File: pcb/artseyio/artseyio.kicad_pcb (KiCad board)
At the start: 2 copper layers, 95.2 x 69.9 mm, 14 parts, among them SW1 SW_MEC_5G, SW2 SW_MEC_5G, SW3 SW_MEC_5G, SW4 SW_MEC_5G, SW5 SW_MEC_5G, SW6 SW_MEC_5G, SW7 SW_MEC_5G, SW8 SW_MEC_5G, U1 RP2040-Zero, U2 mini_esp32

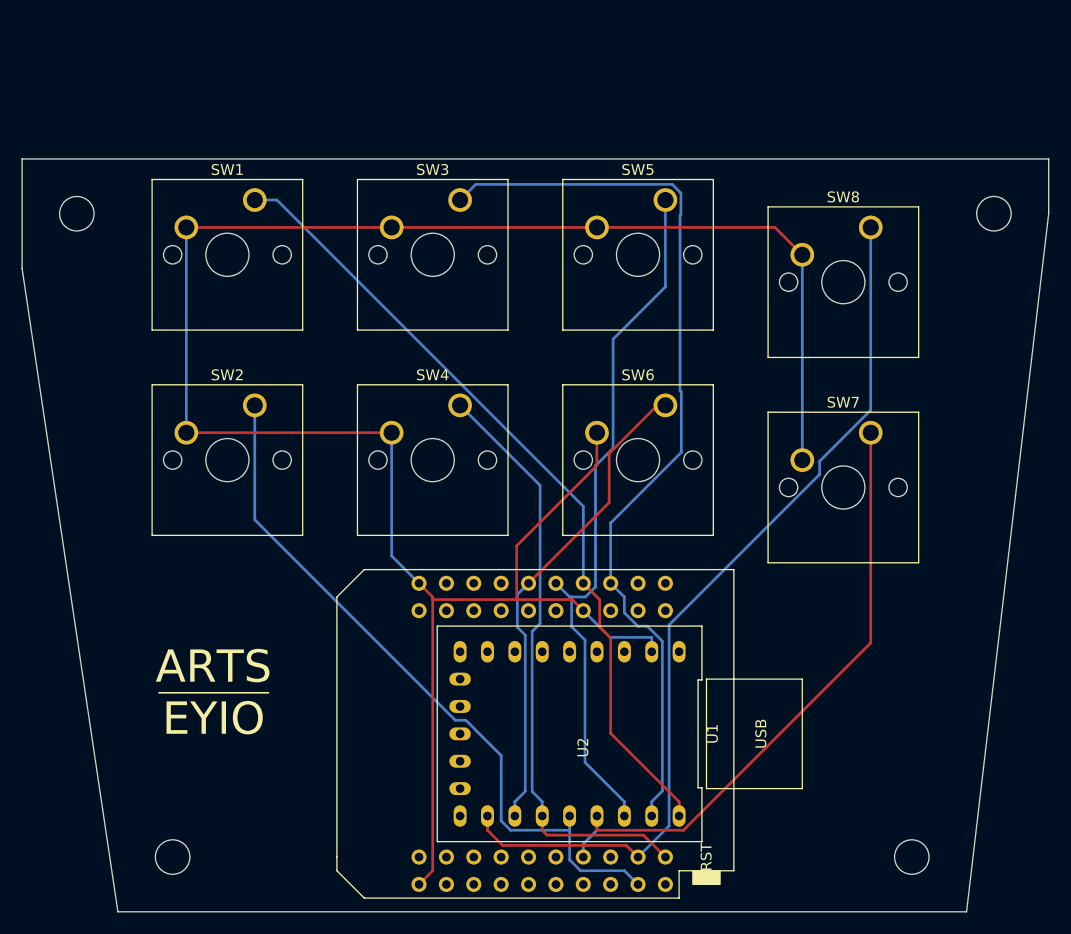
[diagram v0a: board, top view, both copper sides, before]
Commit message: Updated schematic to include  a CH552 with builtin USB-C port.
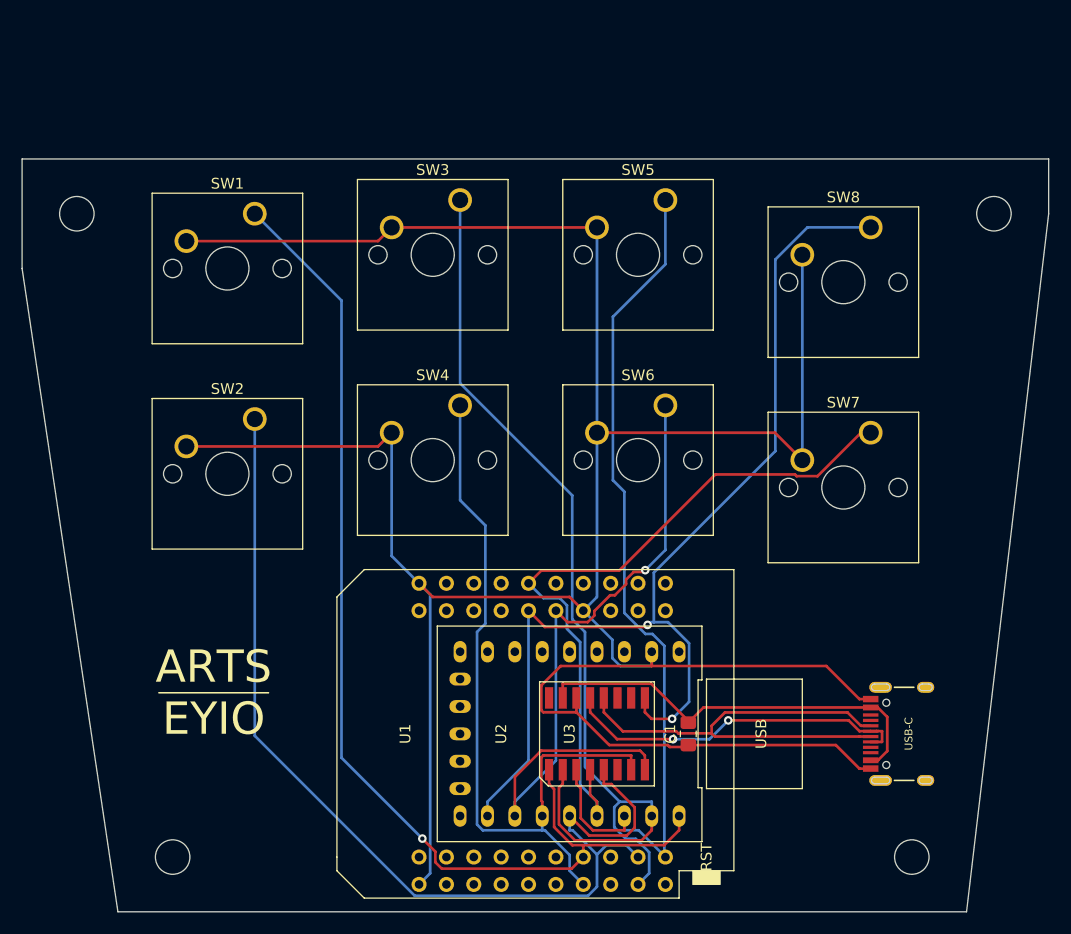
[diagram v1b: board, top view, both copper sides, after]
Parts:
- added C1: C, Capacitor_SMD:C_0805_2012Metric_Pad1.18x1.45mm_HandSolder, F.Cu at (168.5, 118.1)
- added J1: USB_C16PIN, USB-C:USB-C-COM-15111, F.Cu at (185.4, 118.1)
- added U3: CH552G, CH552G:CH552G, F.Cu at (160.0, 118.1)
- moved SW2 1.27 mm to (128.3, 88.9)
- moved SW1 1.27 mm to (128.3, 69.8)
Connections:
- U2 pad 13: unconnected-(U2-Pad13) -> /Y
- U2 pad 14: /S -> /A
- U2 pad 17: /E -> /R
- U2 pad 18: /O -> /E
- U2 pad 20: /Y -> /T
- U2 pad 29: unconnected-(U2-Pad29) -> /O
- U2 pad 30: /I -> /S
- U2 pad 31: unconnected-(U2-Pad31) -> /I
- U2 pad 32: /T -> unconnected-(U2-Pad32)
- U2 pad 34: /A -> unconnected-(U2-Pad34)
- U2 pad 36: /R -> unconnected-(U2-Pad36)
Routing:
- net Earth: track 201.0 -> 274.8 mm
- net Net-(J1-PadA6): track 0.00 -> 43.5 mm
- net Net-(C1-Pad2): track 0.00 -> 39.0 mm
- net Net-(J1-PadA7): track 0.00 -> 32.6 mm, vias 0 -> 2
- net /A: track 74.7 -> 102.3 mm, vias 0 -> 1
- net /E: track 66.7 -> 94.1 mm
- net /I: track 44.9 -> 66.1 mm, vias 0 -> 1
- net /T: track 65.5 -> 82.0 mm
- net /Y: track 55.7 -> 69.7 mm
- net /O: track 83.7 -> 97.3 mm, vias 0 -> 2
- net /S: track 57.8 -> 67.3 mm
- net /R: track 84.9 -> 92.6 mm

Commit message: Updated the footprint shape and updated the ESP32 pinout.
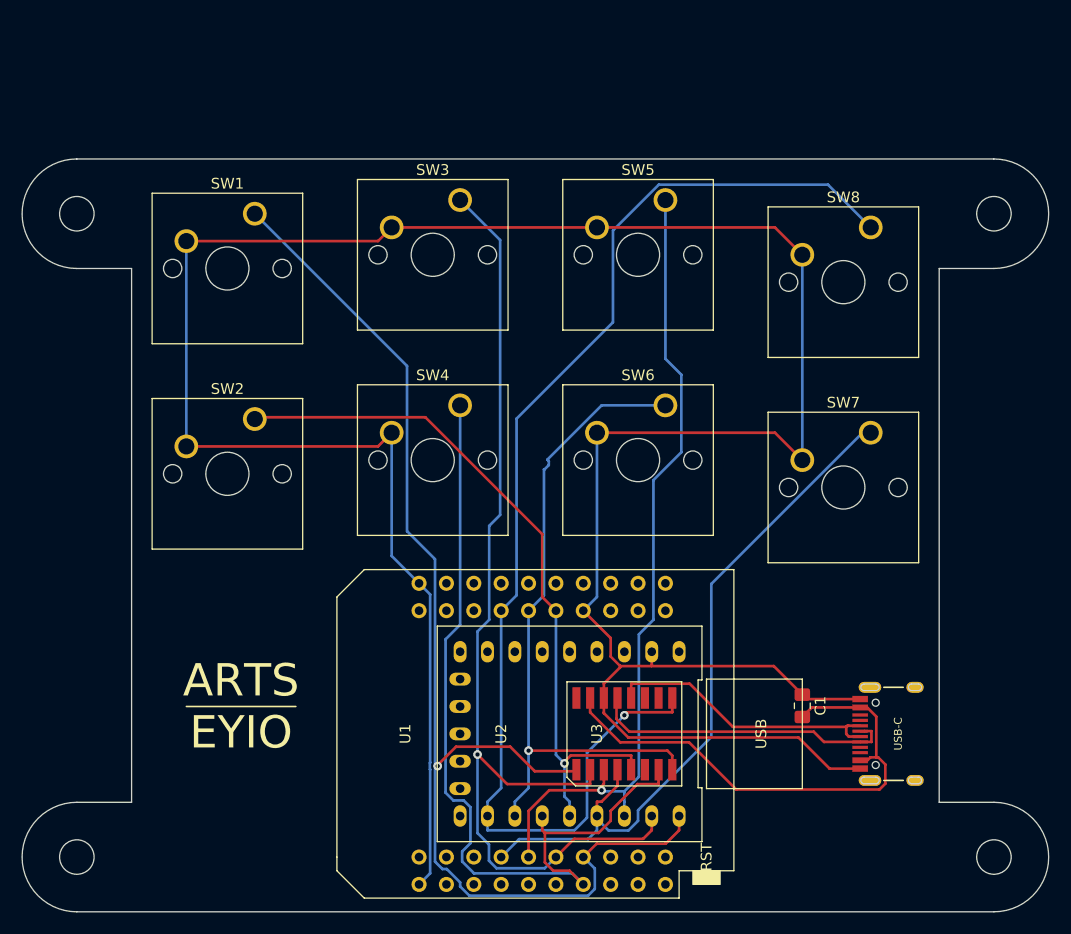
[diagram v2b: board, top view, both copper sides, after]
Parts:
- C1: value C -> 0.1uF
- moved C1 10.9 mm to (179.1, 115.5), turned to -90 degrees
- moved H2 8.89 mm to (111.8, 129.5)
- moved H4 7.62 mm to (196.8, 129.5)
- moved U3 2.54 mm to (162.6, 118.1)
- moved J1 0.99 mm to (184.4, 118.1)
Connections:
- U2 pad 10: unconnected-(U2-Pad10) -> /T
- U2 pad 12: unconnected-(U2-Pad12) -> /R
- U2 pad 17: /R -> unconnected-(U2-Pad17)
- U2 pad 18: /E -> unconnected-(U2-Pad18)
- U2 pad 20: /T -> unconnected-(U2-Pad20)
- U2 pad 27: unconnected-(U2-Pad27) -> /O
- U2 pad 29: /O -> /I
- U2 pad 30: /S -> unconnected-(U2-Pad30)
- U2 pad 31: /I -> /E
- U2 pad 8: unconnected-(U2-Pad8) -> /S
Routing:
- net /E: track 94.1 -> 66.3 mm, vias 0 -> 1
- net Net-(J1-PadA6): track 43.5 -> 26.3 mm
- net /O: track 97.3 -> 114.3 mm, vias 2 -> 1
- net Earth: track 274.8 -> 259.7 mm
- net /A: track 102.3 -> 113.2 mm
- net /Y: track 69.7 -> 79.9 mm
- net Net-(C1-Pad2): track 39.0 -> 47.8 mm
- net /T: track 82.0 -> 75.9 mm, vias 0 -> 1
- net Net-(J1-PadA7): track 32.6 -> 28.6 mm, vias 2 -> 0
- net /I: track 66.1 -> 62.3 mm
- net /R: track 92.6 -> 95.2 mm, vias 0 -> 1
- net /S: track 67.3 -> 66.6 mm
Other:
- outline, holes or cut-outs redrawn

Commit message: Updated reversed switches, rearranged CH552 to reduce vias and USB track length.
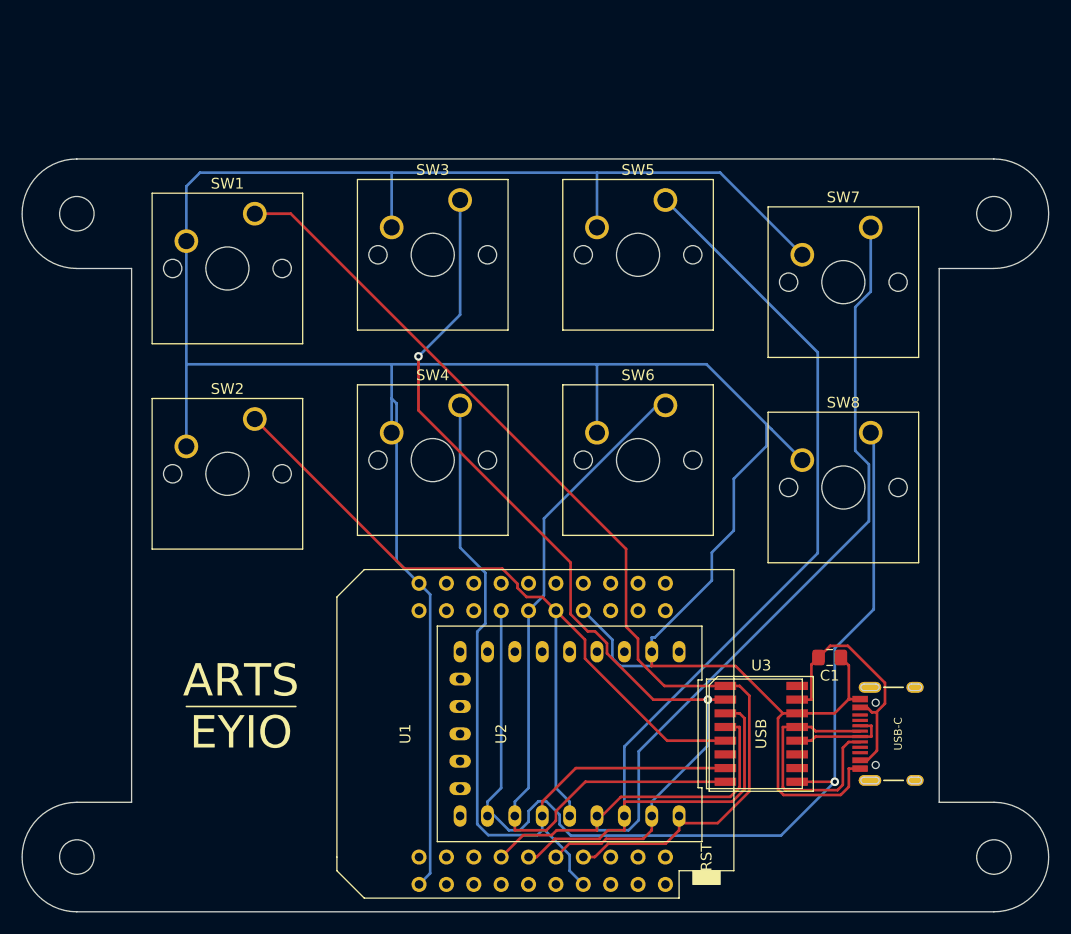
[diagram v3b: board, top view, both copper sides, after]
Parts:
- moved SW7 19.0 mm to (185.4, 71.1)
- moved SW8 19.0 mm to (185.4, 90.2)
- moved U3 12.7 mm to (175.3, 118.1), turned to -90 degrees
- moved C1 5.15 mm to (181.6, 111.0), turned to 180 degrees
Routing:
- net Earth: track 259.7 -> 296.4 mm
- net /S: track 66.6 -> 103.2 mm
- net /T: track 75.9 -> 103.2 mm, vias 1 -> 0
- net Net-(C1-Pad2): track 47.8 -> 23.8 mm
- net /O: track 114.3 -> 95.7 mm
- net Net-(J1-PadA6): track 26.3 -> 9.10 mm
- net /A: track 113.2 -> 97.6 mm, vias 1 -> 0
- net /E: track 66.3 -> 76.8 mm, vias 1 -> 0
- net /R: track 95.2 -> 88.3 mm, vias 1 -> 2
- net /Y: track 79.9 -> 74.5 mm
- net /I: track 62.3 -> 67.6 mm, vias 1 -> 0
- net Net-(J1-PadA7): track 28.6 -> 24.1 mm
